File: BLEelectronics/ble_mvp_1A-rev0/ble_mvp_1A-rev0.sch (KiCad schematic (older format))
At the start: 35 parts, among them IC1 LTC4412xS6, IC2 PCF8523T, IC3 MX25R6435FM2IL0, IC4 LTC4054LES5-4.2#TRPBF, J1 Nordic_nRF52840_breakout, J4 Conn_01x01_Female, Q1 Si2307CDS, Q2 Si7463DP, U1 LP5907MFX-3.3, U2 BAT-HLD-001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

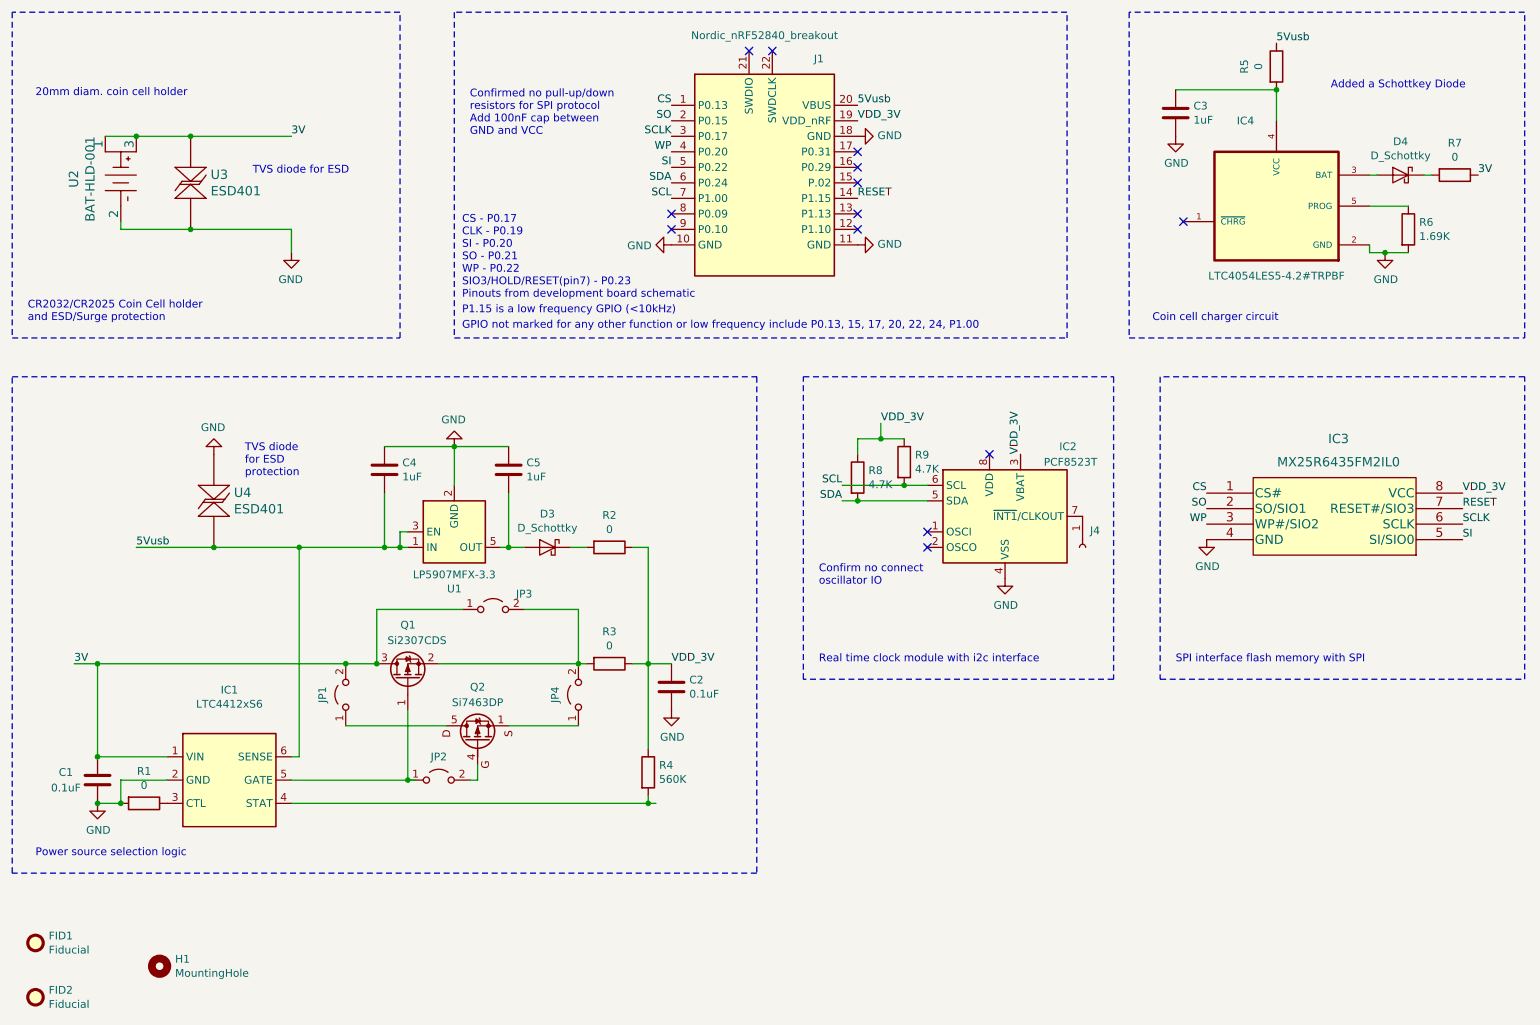
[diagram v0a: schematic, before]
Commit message: correct CS to CS# in schematic and pdfs for all mvps
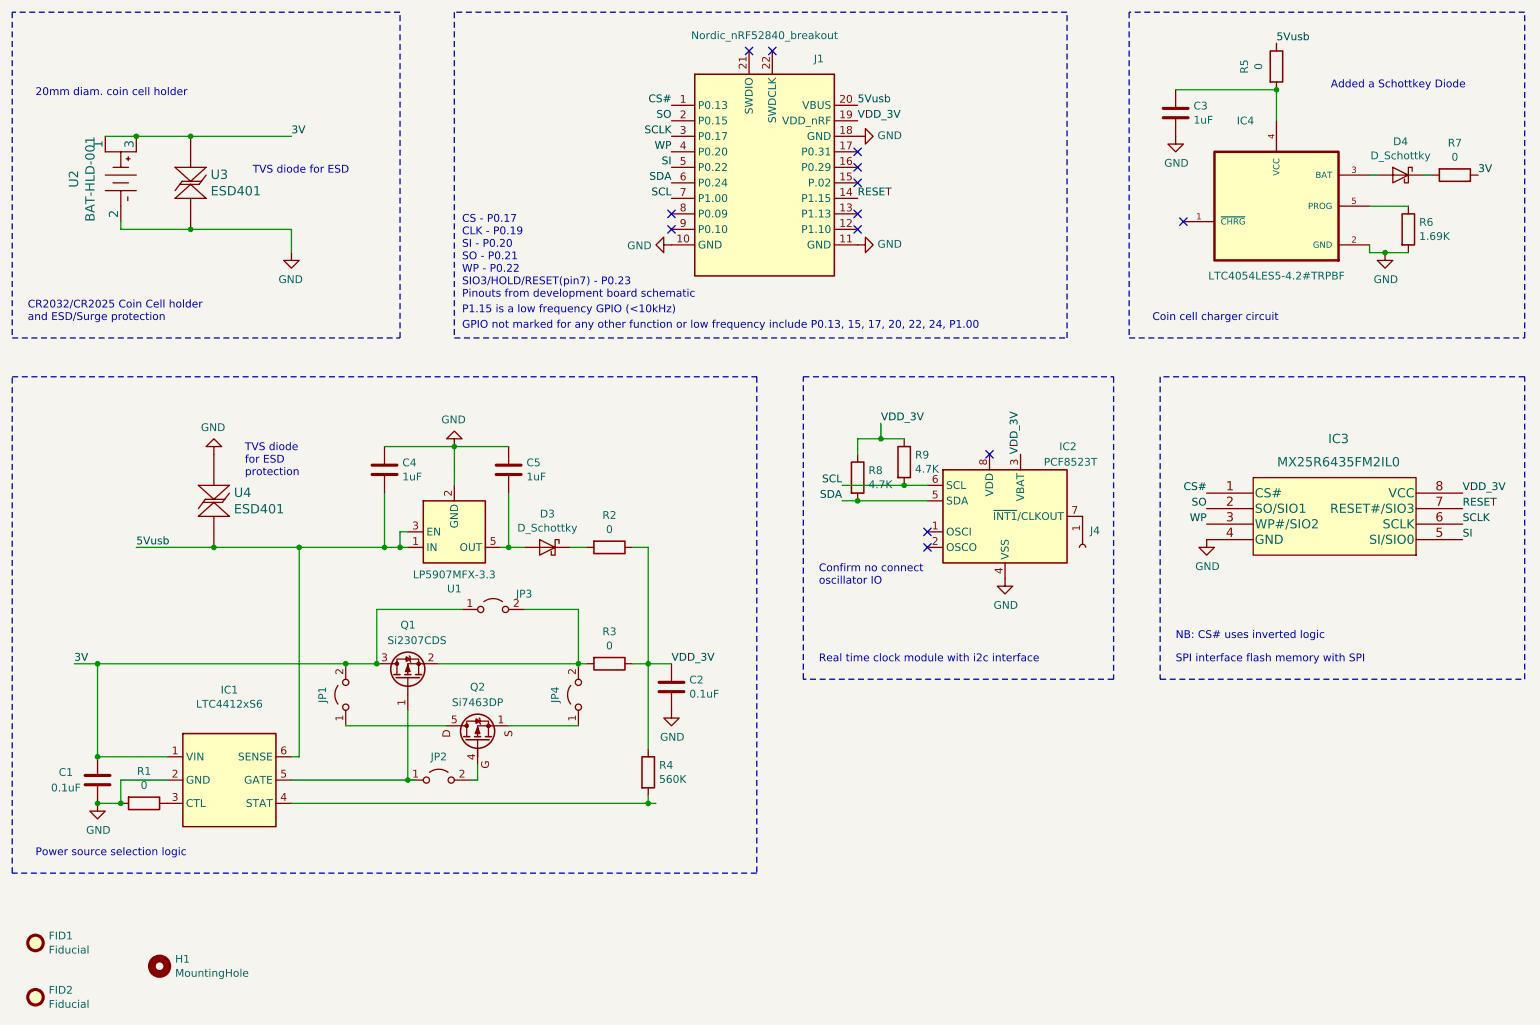
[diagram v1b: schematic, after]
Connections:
- net labels added: CS#
- net labels removed: CS
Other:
- note added: "NB: CS# uses inverted logic"
- note removed: "Confirmed no pull-up/down\nresistors for SPI protocol\nAdd 100nF cap between \nGND and VCC"
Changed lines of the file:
@@
 RESET
 Text Label 8750 4000 2    50   ~ 0
-CS
+CS#
 Text Label 5300 1600 2    50   ~ 0
 SO
 Text Label 5300 1500 2    50   ~ 0
-CS
+CS#
 Text Label 5300 1900 2    50   ~ 0
 SI
@@
 Text Label 8750 4200 2    50   ~ 0
 WP
-Text Notes 4000 1700 0    50   ~ 0
-Confirmed no pull-up/down\nresistors for SPI protocol\nAdd 100nF cap between \nGND and VCC
 Text Label 6650 3550 0    50   ~ 0
 VDD_3V
@@
 Text Notes 3950 2750 0    50   ~ 0
 CS - P0.17\nCLK - P0.19\nSI - P0.20\nSO - P0.21\nWP - P0.22\nSIO3/HOLD/RESET(pin7) - P0.23\nPinouts from development board schematic\n
+Text Notes 8550 4950 0    50   ~ 0
+NB: CS# uses inverted logic
 $EndSCHEMATC

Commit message: Additional changes to schematic labelling.
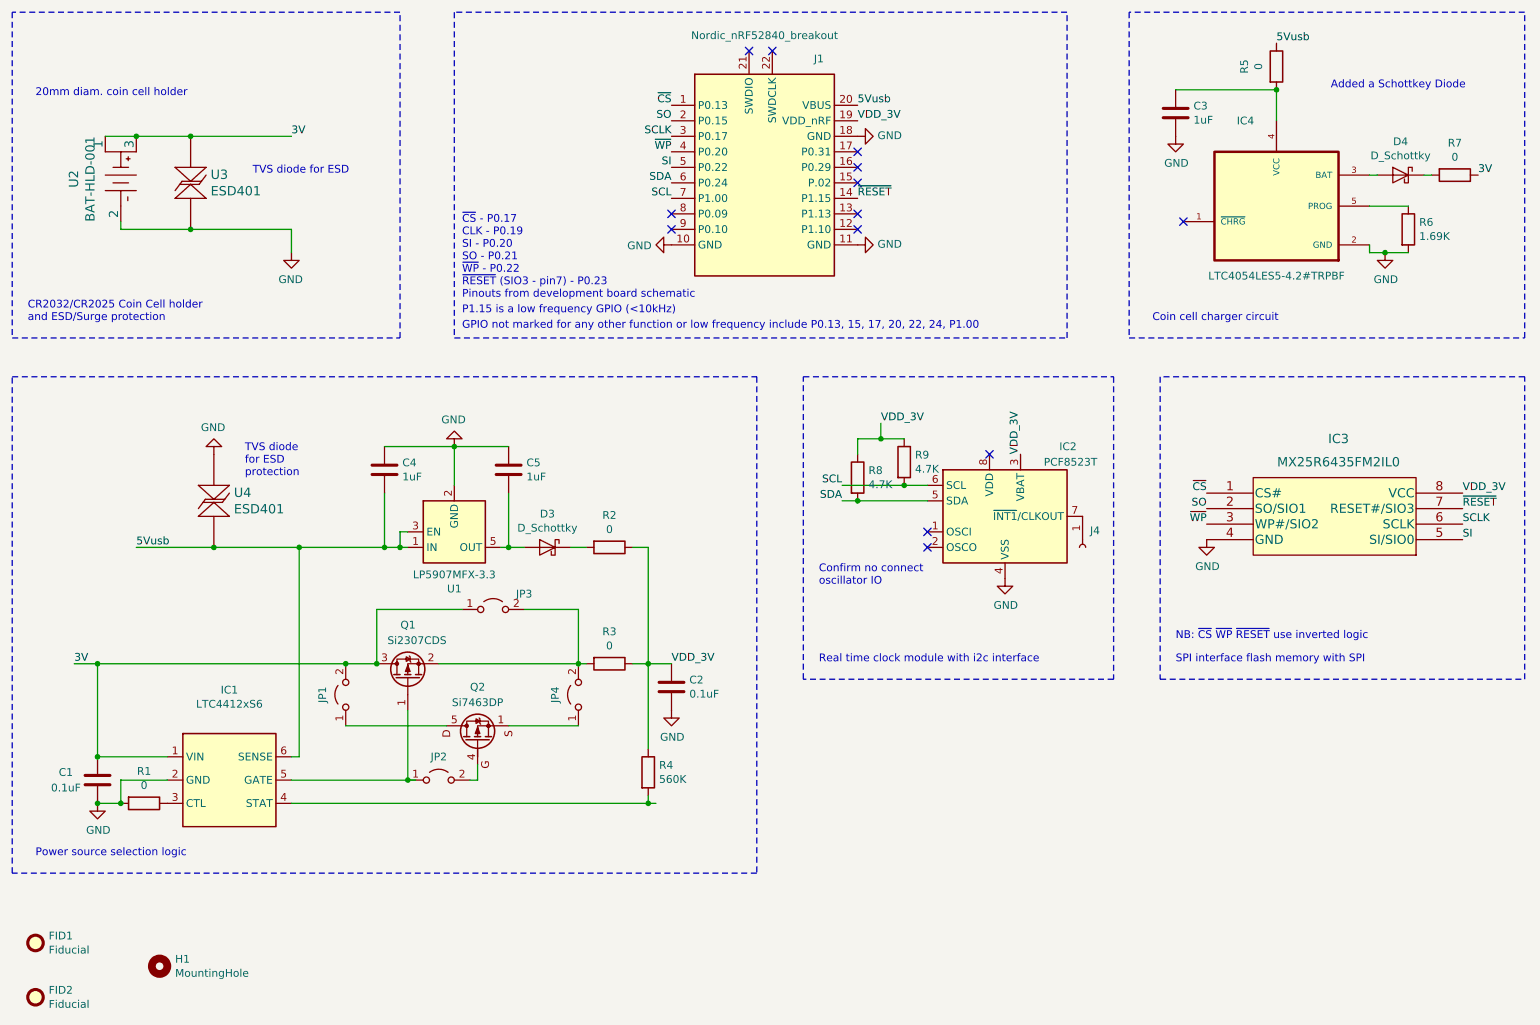
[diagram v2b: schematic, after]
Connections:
- net labels added: ~CS~, ~RESET~, ~WP~
- net labels removed: CS#, RESET, WP
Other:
- note added: "NB: ~CS~ ~WP~ ~RESET~ use inverted logic"
- note added: "~CS~ - P0.17\nCLK - P0.19\nSI - P0.20\nSO - P0.21\n~WP~ - P0.22\n~RESET~ (SIO3 - pin7) - P0.23\nPinouts from development board schematic\n"
- note removed: "CS - P0.17\nCLK - P0.19\nSI - P0.20\nSO - P0.21\nWP - P0.22\nSIO3/HOLD/RESET(pin7) - P0.23\nPinouts from development board schematic\n"
- note removed: "NB: CS# uses inverted logic"
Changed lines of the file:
@@
 SO
 Text Label 10400 4100 0    50   ~ 0
-RESET
+~RESET~
 Text Label 8750 4000 2    50   ~ 0
-CS#
+~CS~
 Text Label 5300 1600 2    50   ~ 0
 SO
 Text Label 5300 1500 2    50   ~ 0
-CS#
+~CS~
 Text Label 5300 1900 2    50   ~ 0
 SI
@@
 P1.15 is a low frequency GPIO (<10kHz)
 Text Label 5300 1800 2    50   ~ 0
-WP
+~WP~
 Text Label 8750 4200 2    50   ~ 0
-WP
+~WP~
 Text Label 6650 3550 0    50   ~ 0
 VDD_3V
@@
 TVS diode \nfor ESD\nprotection
 Text Label 6500 2100 0    50   ~ 0
-RESET
+~RESET~
 Wire Wire Line
 	1650 1700 1850 1700
@@
 	2200 1700 2850 1700
 Text Notes 3950 2750 0    50   ~ 0
-CS - P0.17\nCLK - P0.19\nSI - P0.20\nSO - P0.21\nWP - P0.22\nSIO3/HOLD/RESET(pin7) - P0.23\nPinouts from development board schematic\n
+~CS~ - P0.17\nCLK - P0.19\nSI - P0.20\nSO - P0.21\n~WP~ - P0.22\n~RESET~ (SIO3 - pin7) - P0.23\nPinouts from development board schematic\n
 Text Notes 8550 4950 0    50   ~ 0
-NB: CS# uses inverted logic
+NB: ~CS~ ~WP~ ~RESET~ use inverted logic
 $EndSCHEMATC
